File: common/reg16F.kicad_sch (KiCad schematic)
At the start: 8 parts, among them U17 74AHC1G08, U2 SN74AHCT16374DGGR

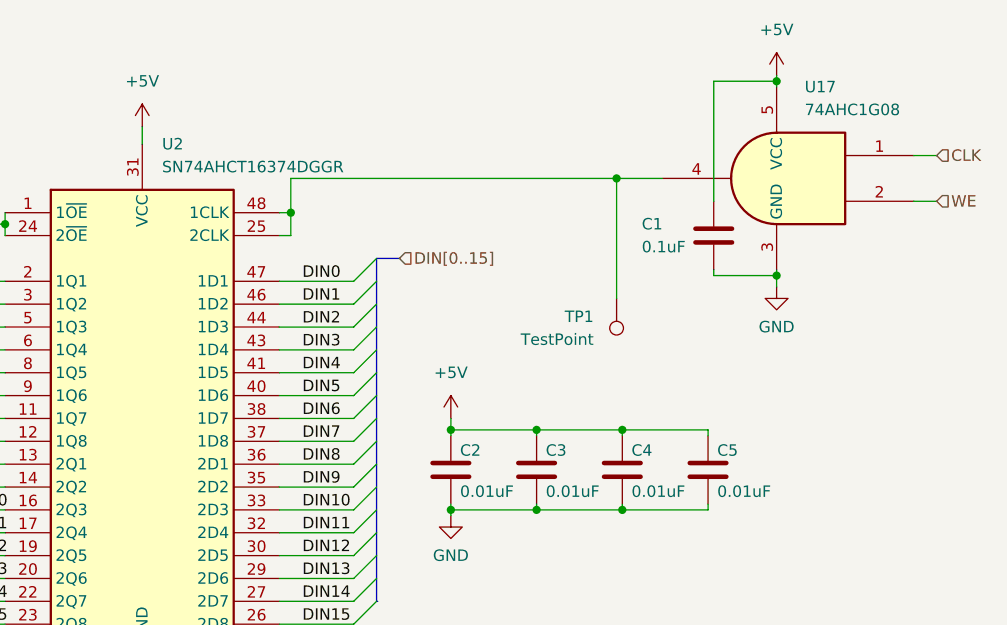
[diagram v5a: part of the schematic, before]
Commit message: Refactored files, finalized reg4x16, and used lowercase v
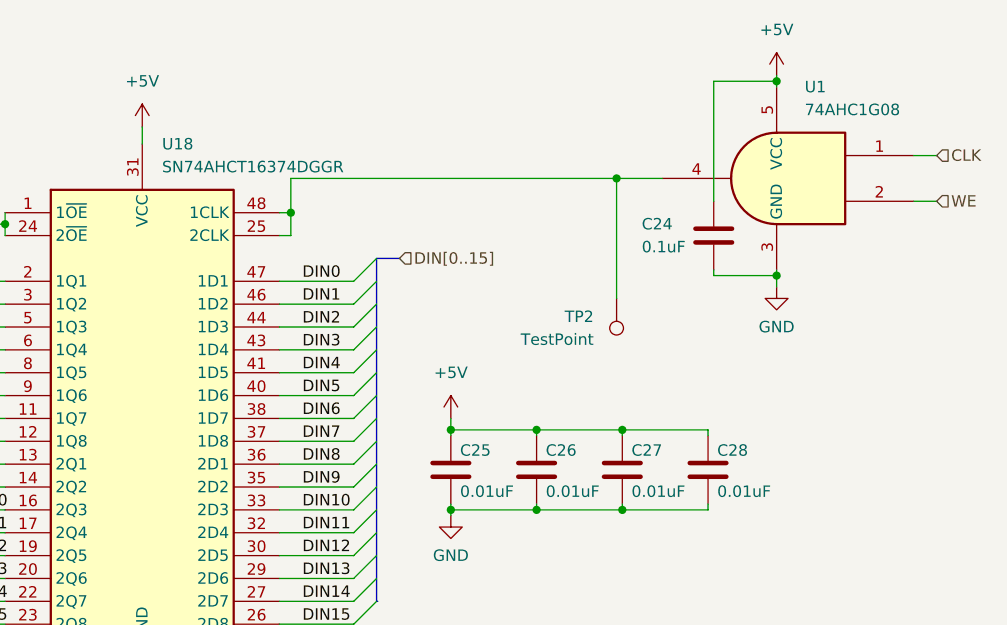
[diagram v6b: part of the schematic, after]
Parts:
- renumbered C1 to C24, C2 to C25, C3 to C26, C4 to C27, C5 to C28, TP1 to TP2, U17 to U1, U2 to U18
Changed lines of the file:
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@@
 		(dnp no)
 		(fields_autoplaced yes)
-		(property "Reference" "#PWR011"
+		(property "Reference" "#PWR039"
 			(at 141.605 95.885 0)
 			(effects
@@
 		)
 		(instances
+			(project "ALU"
+				(path "/a2e955d2-87ce-495b-9d0c-0c0d88eefe1c/7032f906-79dd-4ab6-9425-af002e61fd88"
+					(reference "#PWR039")
+					(unit 1)
+				)
+			)
 			(project "ALU"
 				(path "/c0bb03ae-ed0c-4e9e-9f7c-15f29fb8b868/e88f18b5-e72c-4b0e-9142-9a24ab457305"
@@
 		(dnp no)
 		(fields_autoplaced yes)
-		(property "Reference" "#PWR040"
+		(property "Reference" "#PWR041"
 			(at 107.315 116.84 0)
 			(effects
@@
 		)
 		(instances
+			(project ""
+				(path "/a2e955d2-87ce-495b-9d0c-0c0d88eefe1c/7032f906-79dd-4ab6-9425-af002e61fd88"
+					(reference "#PWR041")
+					(unit 1)
+				)
+			)
 			(project ""
 				(path "/c0bb03ae-ed0c-4e9e-9f7c-15f29fb8b868/e88f18b5-e72c-4b0e-9142-9a24ab457305"
@@
 		(on_board yes)
 		(dnp no)
-		(property "Reference" "C4"
+		(property "Reference" "C27"
 			(at 161.671 82.296 0)
 			(effects
@@
 		)
 		(instances
+			(project "ALU"
+				(path "/a2e955d2-87ce-495b-9d0c-0c0d88eefe1c/7032f906-79dd-4ab6-9425-af002e61fd88"
+					(reference "C27")
+					(unit 1)
+				)
+			)
 			(project "ALU"
 				(path "/c0bb03ae-ed0c-4e9e-9f7c-15f29fb8b868/e88f18b5-e72c-4b0e-9142-9a24ab457305"
@@
 		(on_board yes)
 		(dnp no)
-		(property "Reference" "C2"
+		(property "Reference" "C25"
 			(at 142.621 82.296 0)
 			(effects
@@
 		)
 		(instances
+			(project "ALU"
+				(path "/a2e955d2-87ce-495b-9d0c-0c0d88eefe1c/7032f906-79dd-4ab6-9425-af002e61fd88"
+					(reference "C25")
+					(unit 1)
+				)
+			)
 			(project "ALU"
 				(path "/c0bb03ae-ed0c-4e9e-9f7c-15f29fb8b868/e88f18b5-e72c-4b0e-9142-9a24ab457305"
@@
 		(dnp no)
 		(fields_autoplaced yes)
-		(property "Reference" "U2"
+		(property "Reference" "U18"
 			(at 109.5091 48.26 0)
 			(effects
@@
 		)
 		(instances
+			(project ""
+				(path "/a2e955d2-87ce-495b-9d0c-0c0d88eefe1c/7032f906-79dd-4ab6-9425-af002e61fd88"
+					(reference "U18")
+					(unit 1)
+				)
+			)
 			(project ""
 				(path "/c0bb03ae-ed0c-4e9e-9f7c-15f29fb8b868/e88f18b5-e72c-4b0e-9142-9a24ab457305"
@@
 		(on_board yes)
 		(dnp no)
-		(property "Reference" "C1"
+		(property "Reference" "C24"
 			(at 162.814 57.15 0)
 			(effects
@@
 		)
 		(instances
+			(project "ALU"
+				(path "/a2e955d2-87ce-495b-9d0c-0c0d88eefe1c/7032f906-79dd-4ab6-9425-af002e61fd88"
+					(reference "C24")
+					(unit 1)
+				)
+			)
 			(project "ALU"
 				(path "/c0bb03ae-ed0c-4e9e-9f7c-15f29fb8b868/e88f18b5-e72c-4b0e-9142-9a24ab457305"
@@
 		(on_board yes)
 		(dnp no)
-		(property "Reference" "C5"
+		(property "Reference" "C28"
 			(at 171.196 82.296 0)
 			(effects
@@
 		)
 		(instances
+			(project "ALU"
+				(path "/a2e955d2-87ce-495b-9d0c-0c0d88eefe1c/7032f906-79dd-4ab6-9425-af002e61fd88"
+					(reference "C28")
+					(unit 1)
+				)
+			)
 			(project "ALU"
 				(path "/c0bb03ae-ed0c-4e9e-9f7c-15f29fb8b868/e88f18b5-e72c-4b0e-9142-9a24ab457305"
@@
 		(dnp no)
 		(fields_autoplaced yes)
-		(property "Reference" "TP1"
+		(property "Reference" "TP2"
 			(at 157.48 67.4369 0)
 			(effects
@@
 		)
 		(instances
+			(project "ALU"
+				(path "/a2e955d2-87ce-495b-9d0c-0c0d88eefe1c/7032f906-79dd-4ab6-9425-af002e61fd88"
+					(reference "TP2")
+					(unit 1)
+				)
+			)
 			(project "ALU"
 				(path "/c0bb03ae-ed0c-4e9e-9f7c-15f29fb8b868/e88f18b5-e72c-4b0e-9142-9a24ab457305"
@@
 		(dnp no)
 		(fields_autoplaced yes)
-		(property "Reference" "#PWR036"
+		(property "Reference" "#PWR037"
 			(at 107.315 50.165 0)
 			(effects
@@
 		)
 		(instances
+			(project "ALU"
+				(path "/a2e955d2-87ce-495b-9d0c-0c0d88eefe1c/7032f906-79dd-4ab6-9425-af002e61fd88"
+					(reference "#PWR037")
+					(unit 1)
+				)
+			)
 			(project "ALU"
 				(path "/c0bb03ae-ed0c-4e9e-9f7c-15f29fb8b868/e88f18b5-e72c-4b0e-9142-9a24ab457305"
@@
 		(on_board yes)
 		(dnp no)
-		(property "Reference" "C3"
+		(property "Reference" "C26"
 			(at 152.146 82.296 0)
 			(effects
@@
 		)
 		(instances
+			(project "ALU"
+				(path "/a2e955d2-87ce-495b-9d0c-0c0d88eefe1c/7032f906-79dd-4ab6-9425-af002e61fd88"
+					(reference "C26")
+					(unit 1)
+				)
+			)
 			(project "ALU"
 				(path "/c0bb03ae-ed0c-4e9e-9f7c-15f29fb8b868/e88f18b5-e72c-4b0e-9142-9a24ab457305"
@@
 		(dnp no)
 		(fields_autoplaced yes)
-		(property "Reference" "#PWR06"
+		(property "Reference" "#PWR0106"
 			(at 177.8 44.45 0)
 			(effects
@@
 		)
 		(instances
+			(project "ALU"
+				(path "/a2e955d2-87ce-495b-9d0c-0c0d88eefe1c/7032f906-79dd-4ab6-9425-af002e61fd88"
+					(reference "#PWR0106")
+					(unit 1)
+				)
+			)
 			(project "ALU"
 				(path "/c0bb03ae-ed0c-4e9e-9f7c-15f29fb8b868/e88f18b5-e72c-4b0e-9142-9a24ab457305"
@@
 		(dnp no)
 		(fields_autoplaced yes)
-		(property "Reference" "#PWR07"
+		(property "Reference" "#PWR0107"
 			(at 177.8 70.485 0)
 			(effects
@@
 		)
 		(instances
+			(project "ALU"
+				(path "/a2e955d2-87ce-495b-9d0c-0c0d88eefe1c/7032f906-79dd-4ab6-9425-af002e61fd88"
+					(reference "#PWR0107")
+					(unit 1)
+				)
+			)
 			(project "ALU"
 				(path "/c0bb03ae-ed0c-4e9e-9f7c-15f29fb8b868/e88f18b5-e72c-4b0e-9142-9a24ab457305"
@@
 		(dnp no)
 		(fields_autoplaced yes)
-		(property "Reference" "U17"
+		(property "Reference" "U1"
 			(at 180.9181 41.91 0)
 			(effects
@@
 		)
 		(instances
+			(project "ALU"
+				(path "/a2e955d2-87ce-495b-9d0c-0c0d88eefe1c/7032f906-79dd-4ab6-9425-af002e61fd88"
+					(reference "U1")
+					(unit 1)
+				)
+			)
 			(project "ALU"
 				(path "/c0bb03ae-ed0c-4e9e-9f7c-15f29fb8b868/e88f18b5-e72c-4b0e-9142-9a24ab457305"
@@
 		(dnp no)
 		(fields_autoplaced yes)
-		(property "Reference" "#PWR010"
+		(property "Reference" "#PWR038"
 			(at 141.605 82.55 0)
 			(effects
@@
 		(instances
 			(project "ALU"
-				(path "/c0bb03ae-ed0c-4e9e-9f7c-15f29fb8b868/e88f18b5-e72c-4b0e-9142-9a24ab457305"
+				(path "/a2e955d2-87ce-495b-9d0c-0c0d88eefe1c/7032f906-79dd-4ab6-9425-af002e61fd88"
+					(reference "#PWR038")
+					(unit 1)
+				)
+			)
+			(project "ALU"
+				(path "/c0bb03ae-ed0c-4e9e-9f7c-15f29fb8b868/e88f18b5-e72c-4b0e-9142-9a24ab457305"

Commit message: Memory Controller- Initial setup
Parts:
- renumbered C25 to C10, C26 to C11, C27 to C12, C28 to C13, C24 to C14, TP2 to TP1, U18 to U10, U1 to U11
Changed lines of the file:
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@@
 		(dnp no)
 		(fields_autoplaced yes)
-		(property "Reference" "#PWR039"
+		(property "Reference" "#PWR0103"
 			(at 141.605 95.885 0)
 			(effects
@@
 		)
 		(instances
-			(project "ALU"
-				(path "/a2e955d2-87ce-495b-9d0c-0c0d88eefe1c/7032f906-79dd-4ab6-9425-af002e61fd88"
-					(reference "#PWR039")
+			(project "Memory Controller"
+				(path "/a2e955d2-87ce-495b-9d0c-0c0d88eefe1c/7032f906-79dd-4ab6-9425-af002e61fd88"
+					(reference "#PWR0103")
 					(unit 1)
 				)
@@
 		(dnp no)
 		(fields_autoplaced yes)
-		(property "Reference" "#PWR041"
+		(property "Reference" "#PWR023"
 			(at 107.315 116.84 0)
 			(effects
@@
 			(project ""
 				(path "/a2e955d2-87ce-495b-9d0c-0c0d88eefe1c/7032f906-79dd-4ab6-9425-af002e61fd88"
-					(reference "#PWR041")
+					(reference "#PWR023")
 					(unit 1)
 				)
@@
 		(on_board yes)
 		(dnp no)
-		(property "Reference" "C27"
+		(property "Reference" "C12"
 			(at 161.671 82.296 0)
 			(effects
@@
 		)
 		(instances
-			(project "ALU"
-				(path "/a2e955d2-87ce-495b-9d0c-0c0d88eefe1c/7032f906-79dd-4ab6-9425-af002e61fd88"
-					(reference "C27")
+			(project "Memory Controller"
+				(path "/a2e955d2-87ce-495b-9d0c-0c0d88eefe1c/7032f906-79dd-4ab6-9425-af002e61fd88"
+					(reference "C12")
 					(unit 1)
 				)
@@
 		(on_board yes)
 		(dnp no)
-		(property "Reference" "C25"
+		(property "Reference" "C10"
 			(at 142.621 82.296 0)
 			(effects
@@
 		)
 		(instances
-			(project "ALU"
-				(path "/a2e955d2-87ce-495b-9d0c-0c0d88eefe1c/7032f906-79dd-4ab6-9425-af002e61fd88"
-					(reference "C25")
+			(project "Memory Controller"
+				(path "/a2e955d2-87ce-495b-9d0c-0c0d88eefe1c/7032f906-79dd-4ab6-9425-af002e61fd88"
+					(reference "C10")
 					(unit 1)
 				)
@@
 		(dnp no)
 		(fields_autoplaced yes)
-		(property "Reference" "U18"
-			(at 109.5091 48.26 0)
+		(property "Reference" "U10"
+			(at 109.4583 48.26 0)
 			(effects
 				(font
@@
 		)
 		(property "Value" "SN74AHCT16374DGGR"
-			(at 109.5091 50.8 0)
+			(at 109.4583 50.8 0)
 			(effects
 				(font
@@
 			(project ""
 				(path "/a2e955d2-87ce-495b-9d0c-0c0d88eefe1c/7032f906-79dd-4ab6-9425-af002e61fd88"
-					(reference "U18")
+					(reference "U10")
 					(unit 1)
 				)
@@
 		(on_board yes)
 		(dnp no)
-		(property "Reference" "C24"
+		(property "Reference" "C14"
 			(at 162.814 57.15 0)
 			(effects
@@
 		)
 		(instances
-			(project "ALU"
-				(path "/a2e955d2-87ce-495b-9d0c-0c0d88eefe1c/7032f906-79dd-4ab6-9425-af002e61fd88"
-					(reference "C24")
+			(project "Memory Controller"
+				(path "/a2e955d2-87ce-495b-9d0c-0c0d88eefe1c/7032f906-79dd-4ab6-9425-af002e61fd88"
+					(reference "C14")
 					(unit 1)
 				)
@@
 		(on_board yes)
 		(dnp no)
-		(property "Reference" "C28"
+		(property "Reference" "C13"
 			(at 171.196 82.296 0)
 			(effects
@@
 		)
 		(instances
-			(project "ALU"
-				(path "/a2e955d2-87ce-495b-9d0c-0c0d88eefe1c/7032f906-79dd-4ab6-9425-af002e61fd88"
-					(reference "C28")
+			(project "Memory Controller"
+				(path "/a2e955d2-87ce-495b-9d0c-0c0d88eefe1c/7032f906-79dd-4ab6-9425-af002e61fd88"
+					(reference "C13")
 					(unit 1)
 				)
@@
 		(dnp no)
 		(fields_autoplaced yes)
-		(property "Reference" "TP2"
+		(property "Reference" "TP1"
 			(at 157.48 67.4369 0)
 			(effects
@@
 		)
 		(instances
-			(project "ALU"
-				(path "/a2e955d2-87ce-495b-9d0c-0c0d88eefe1c/7032f906-79dd-4ab6-9425-af002e61fd88"
-					(reference "TP2")
+			(project "Memory Controller"
+				(path "/a2e955d2-87ce-495b-9d0c-0c0d88eefe1c/7032f906-79dd-4ab6-9425-af002e61fd88"
+					(reference "TP1")
 					(unit 1)
 				)
@@
 		(dnp no)
 		(fields_autoplaced yes)
-		(property "Reference" "#PWR037"
+		(property "Reference" "#PWR0102"
 			(at 107.315 50.165 0)
 			(effects
@@
 		)
 		(instances
-			(project "ALU"
-				(path "/a2e955d2-87ce-495b-9d0c-0c0d88eefe1c/7032f906-79dd-4ab6-9425-af002e61fd88"
-					(reference "#PWR037")
+			(project "Memory Controller"
+				(path "/a2e955d2-87ce-495b-9d0c-0c0d88eefe1c/7032f906-79dd-4ab6-9425-af002e61fd88"
+					(reference "#PWR0102")
 					(unit 1)
 				)
@@
 		(on_board yes)
 		(dnp no)
-		(property "Reference" "C26"
+		(property "Reference" "C11"
 			(at 152.146 82.296 0)
 			(effects
@@
 		)
 		(instances
-			(project "ALU"
-				(path "/a2e955d2-87ce-495b-9d0c-0c0d88eefe1c/7032f906-79dd-4ab6-9425-af002e61fd88"
-					(reference "C26")
+			(project "Memory Controller"
+				(path "/a2e955d2-87ce-495b-9d0c-0c0d88eefe1c/7032f906-79dd-4ab6-9425-af002e61fd88"
+					(reference "C11")
 					(unit 1)
 				)
@@
 		(dnp no)
 		(fields_autoplaced yes)
-		(property "Reference" "#PWR0106"
+		(property "Reference" "#PWR0104"
 			(at 177.8 44.45 0)
 			(effects
@@
 		)
 		(instances
-			(project "ALU"
-				(path "/a2e955d2-87ce-495b-9d0c-0c0d88eefe1c/7032f906-79dd-4ab6-9425-af002e61fd88"
-					(reference "#PWR0106")
+			(project "Memory Controller"
+				(path "/a2e955d2-87ce-495b-9d0c-0c0d88eefe1c/7032f906-79dd-4ab6-9425-af002e61fd88"
+					(reference "#PWR0104")
 					(unit 1)
 				)
@@
 		(dnp no)
 		(fields_autoplaced yes)
-		(property "Reference" "#PWR0107"
+		(property "Reference" "#PWR0105"
 			(at 177.8 70.485 0)
 			(effects
@@
 		)
 		(instances
-			(project "ALU"
-				(path "/a2e955d2-87ce-495b-9d0c-0c0d88eefe1c/7032f906-79dd-4ab6-9425-af002e61fd88"
-					(reference "#PWR0107")
+			(project "Memory Controller"
+				(path "/a2e955d2-87ce-495b-9d0c-0c0d88eefe1c/7032f906-79dd-4ab6-9425-af002e61fd88"
+					(reference "#PWR0105")
 					(unit 1)
 				)
@@
 		(dnp no)
 		(fields_autoplaced yes)
-		(property "Reference" "U1"
+		(property "Reference" "U11"
 			(at 180.9181 41.91 0)
 			(effects
@@
 		)
 		(instances
-			(project "ALU"
-				(path "/a2e955d2-87ce-495b-9d0c-0c0d88eefe1c/7032f906-79dd-4ab6-9425-af002e61fd88"
-					(reference "U1")
+			(project "Memory Controller"
+				(path "/a2e955d2-87ce-495b-9d0c-0c0d88eefe1c/7032f906-79dd-4ab6-9425-af002e61fd88"
+					(reference "U11")
 					(unit 1)
 				)
@@
 		(dnp no)
 		(fields_autoplaced yes)
-		(property "Reference" "#PWR038"
+		(property "Reference" "#PWR0101"
 			(at 141.605 82.55 0)
 			(effects
@@
 		)
 		(instances
-			(project "ALU"
-				(path "/a2e955d2-87ce-495b-9d0c-0c0d88eefe1c/7032f906-79dd-4ab6-9425-af002e61fd88"
-					(reference "#PWR038")
-					(unit 1)
-				)
+			(project "Memory Controller"
+				(path "/a2e955d2-87ce-495b-9d0c-0c0d88eefe1c/7032f906-79dd-4ab6-9425-af002e61fd88"
+					(reference "#PWR0101")
+					(unit 1)
+				)
